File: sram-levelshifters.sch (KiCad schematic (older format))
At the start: 15 parts, among them U10 TXB0108-PW, U11 ISSI61WV5128BL, U12 ISSI61WV5128BL, U13 ISSI61WV5128BL, U14 ISSI61WV5128BL, U4 TXB0108-PW, U5 TXB0108-PW, U6 TXB0108-PW, U7 74HC04, U8 TXB0108-PW, U9 74LS32

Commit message: Revised logic using nOE and R/nW as supposed to be...
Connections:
- net mR/~W: now also U7.3
- net ~mOE: now reaches U7.4
- net ~mOE: now also U11.24 (~OE), U12.24 (~OE), U13.24 (~OE), U14.24 (~OE)
- removed net ~ADDRESS_SELECTOR: U11.24 (~OE), U12.24 (~OE), U13.24 (~OE), U14.24 (~OE), U9.3
- new net ~ADDRSEL16K: U9.3
- no-connect marks 31 -> 29
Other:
- moved on the sheet: U7B, U7C, U7D, U7E, U7F
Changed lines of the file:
@@
 Text Notes 6450 800  0    59   ~ 12
 STATIC RAM
-Text GLabel 8350 2650 3    39   BiDi ~ 8
-~ADDRESS_SELECTOR
-Text GLabel 10000 2650 3    39   BiDi ~ 8
-~ADDRESS_SELECTOR
-Text GLabel 10000 5550 3    39   BiDi ~ 8
-~ADDRESS_SELECTOR
-Text GLabel 8350 5550 3    39   BiDi ~ 8
-~ADDRESS_SELECTOR
 Text GLabel 5000 4100 2    39   BiDi ~ 8
-~ADDRESS_SELECTOR
+~ADDRSEL16K
 $Comp
 L 74LS32 U9
@@
 L 74HC04 U7
 U 2 1 5C2DFEE1
-P 3600 4450
-F 0 "U7" H 3600 4500 50  0000 C CNN
-F 1 "74HC04" H 3600 4400 50  0000 C CNN
-F 2 "Housings_SSOP:TSSOP-14_4.4x5mm_Pitch0.65mm" H 3600 4450 50  0001 C CNN
-F 3 "" H 3600 4450 50  0001 C CNN
-	2    3600 4450
+P 4600 4500
+F 0 "U7" H 4600 4550 50  0000 C CNN
+F 1 "74HC04" H 4600 4450 50  0000 C CNN
+F 2 "Housings_SSOP:TSSOP-14_4.4x5mm_Pitch0.65mm" H 4600 4500 50  0001 C CNN
+F 3 "" H 4600 4500 50  0001 C CNN
+	2    4600 4500
 	1    0    0    -1
 $EndComp
@@
 L 74HC04 U7
 U 3 1 5C2DFF28
-P 4350 4450
-F 0 "U7" H 4350 4500 50  0000 C CNN
-F 1 "74HC04" H 4350 4400 50  0000 C CNN
-F 2 "Housings_SSOP:TSSOP-14_4.4x5mm_Pitch0.65mm" H 4350 4450 50  0001 C CNN
-F 3 "" H 4350 4450 50  0001 C CNN
-	3    4350 4450
-	1    0    0    -1
+P 5850 4800
+F 0 "U7" H 5850 4850 50  0000 C CNN
+F 1 "74HC04" H 5850 4750 50  0000 C CNN
+F 2 "Housings_SSOP:TSSOP-14_4.4x5mm_Pitch0.65mm" H 5850 4800 50  0001 C CNN
+F 3 "" H 5850 4800 50  0001 C CNN
+	3    5850 4800
+	0    1    1    0
 $EndComp
 $Comp
 L 74HC04 U7
 U 4 1 5C2E0001
-P 5100 4450
-F 0 "U7" H 5100 4500 50  0000 C CNN
-F 1 "74HC04" H 5100 4400 50  0000 C CNN
-F 2 "Housings_SSOP:TSSOP-14_4.4x5mm_Pitch0.65mm" H 5100 4450 50  0001 C CNN
-F 3 "" H 5100 4450 50  0001 C CNN
-	4    5100 4450
-	1    0    0    -1
-$EndComp
-NoConn ~ 5400 4450
-NoConn ~ 4800 4450
-NoConn ~ 4650 4450
-NoConn ~ 4050 4450
-NoConn ~ 3900 4450
-NoConn ~ 3300 4450
+P 5850 5550
+F 0 "U7" H 5850 5600 50  0000 C CNN
+F 1 "74HC04" H 5850 5500 50  0000 C CNN
+F 2 "Housings_SSOP:TSSOP-14_4.4x5mm_Pitch0.65mm" H 5850 5550 50  0001 C CNN
+F 3 "" H 5850 5550 50  0001 C CNN
+	4    5850 5550
+	0    1    1    0
+$EndComp
+NoConn ~ 5850 4500
+NoConn ~ 5850 5100
+NoConn ~ 5850 5250
+NoConn ~ 5850 5850
 $Comp
 L 74HC04 U7
 U 5 1 5C2E0114
-P 5800 4550
-F 0 "U7" H 5800 4600 50  0000 C CNN
-F 1 "74HC04" H 5800 4500 50  0000 C CNN
-F 2 "Housings_SSOP:TSSOP-14_4.4x5mm_Pitch0.65mm" H 5800 4550 50  0001 C CNN
-F 3 "" H 5800 4550 50  0001 C CNN
-	5    5800 4550
+P 5850 6300
+F 0 "U7" H 5850 6350 50  0000 C CNN
+F 1 "74HC04" H 5850 6250 50  0000 C CNN
+F 2 "Housings_SSOP:TSSOP-14_4.4x5mm_Pitch0.65mm" H 5850 6300 50  0001 C CNN
+F 3 "" H 5850 6300 50  0001 C CNN
+	5    5850 6300
 	0    1    1    0
 $EndComp
@@
 L 74HC04 U7
 U 6 1 5C2E0161
-P 5750 5400
-F 0 "U7" H 5750 5450 50  0000 C CNN
-F 1 "74HC04" H 5750 5350 50  0000 C CNN
-F 2 "Housings_SSOP:TSSOP-14_4.4x5mm_Pitch0.65mm" H 5750 5400 50  0001 C CNN
-F 3 "" H 5750 5400 50  0001 C CNN
-	6    5750 5400
-	0    1    1    0
-$EndComp
-NoConn ~ 5800 4250
-NoConn ~ 5800 4850
-NoConn ~ 5750 5100
-NoConn ~ 5750 5700
+P 5850 7050
+F 0 "U7" H 5850 7100 50  0000 C CNN
+F 1 "74HC04" H 5850 7000 50  0000 C CNN
+F 2 "Housings_SSOP:TSSOP-14_4.4x5mm_Pitch0.65mm" H 5850 7050 50  0001 C CNN
+F 3 "" H 5850 7050 50  0001 C CNN
+	6    5850 7050
+	0    1    1    0
+$EndComp
+NoConn ~ 5850 6000
+NoConn ~ 5850 6600
+NoConn ~ 5850 6750
+NoConn ~ 5850 7350
 $Comp
 L 74HC04 U7
@@
 Text GLabel 7150 6050 0    39   BiDi ~ 0
 PB4
+Text GLabel 4300 4500 0    39   BiDi ~ 0
+mR/~W
+Text GLabel 4900 4500 2    39   BiDi ~ 0
+~mOE
+Text GLabel 8350 2650 3    39   BiDi ~ 0
+~mOE
+Text GLabel 10000 2650 3    39   BiDi ~ 0
+~mOE
+Text GLabel 10000 5550 3    39   BiDi ~ 0
+~mOE
+Text GLabel 8350 5550 3    39   BiDi ~ 0
+~mOE
 $EndSCHEMATC

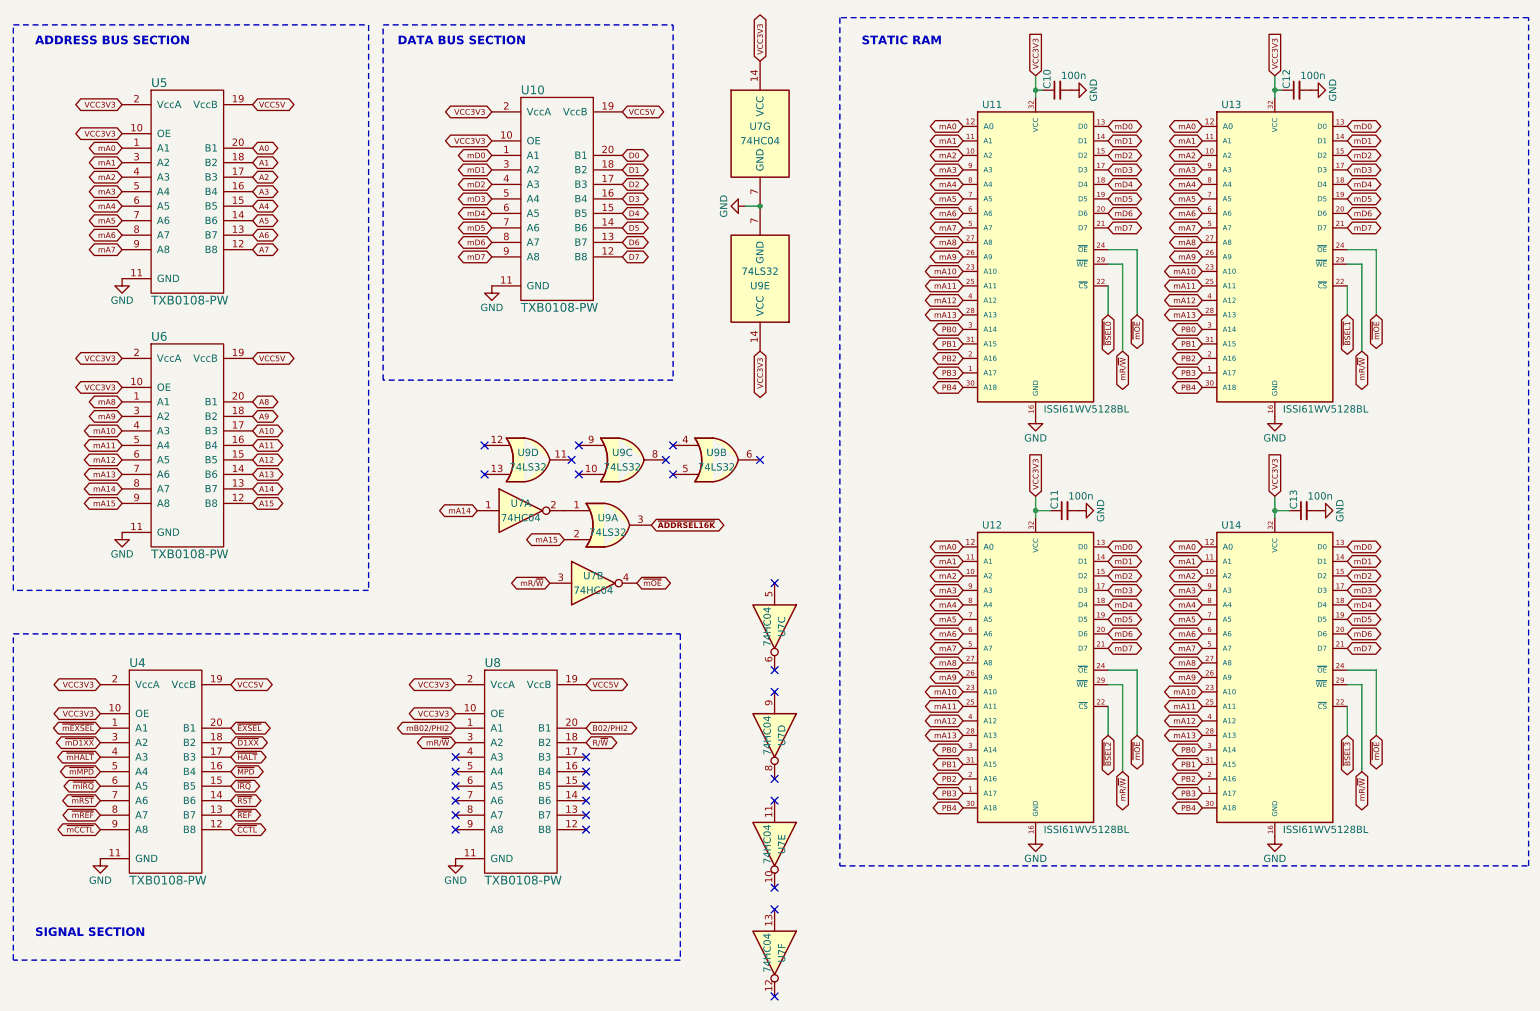
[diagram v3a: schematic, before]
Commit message: Changed the bankselection $D530 and bankcontrol $D531
Changed the bankselection $D530 and bankcontrol $D531
Now in this way, only nCCTL can be used as address selector and only low
byte address is needed in the SoC
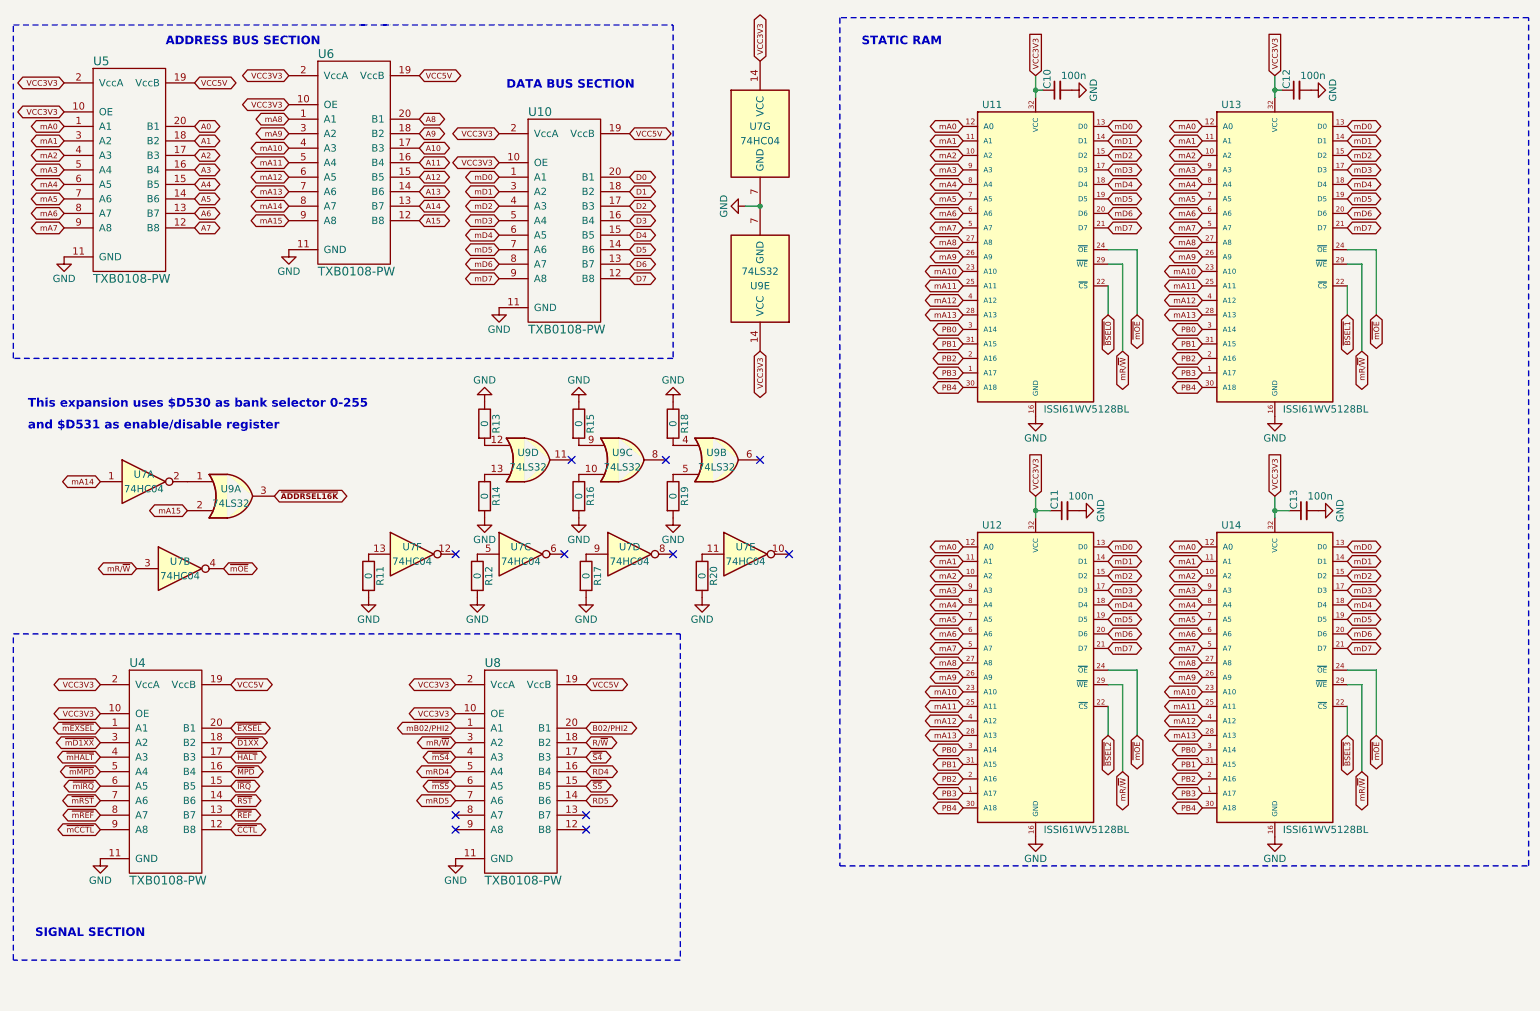
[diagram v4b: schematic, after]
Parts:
- added R11, R12, R13, R14, R15, R16, R17, R18, R19, R20: 0, Resistors_SMD:R_1206_HandSoldering, symbol R
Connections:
- net GND: now also R11.2, R12.2, R13.1, R14.2, R15.1, R16.2, R17.2, R18.1, R19.2, R20.2
- net RD5: now reaches U8.14 (B6)
- net ~S5: now reaches U8.15 (B5)
- net RD4: now reaches U8.16 (B4)
- net ~S4: now reaches U8.17 (B3)
- net ~mS4: now reaches U8.4 (A3)
- net mRD4: now reaches U8.5 (A4)
- net ~mS5: now reaches U8.6 (A5)
- net mRD5: now reaches U8.7 (A6)
- net at U9.4: now also R18.2
- net at U9.5: now also R19.1
- net at U9.10: now also R16.1
- net at U9.9: now also R15.2
- net at U9.12: now also R13.2
- net at U9.13: now also R14.1
- net at U7.5: now also R12.1
- net at U7.9: now also R17.1
- net at U7.11: now also R20.1
- net at U7.13: now also R11.1
- no-connect marks 29 -> 11
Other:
- note added: "This expansion uses $D530 as bank selector 0-255"
- note added: "and $D531 as enable/disable register"
- moved on the sheet: U10, U5, U7A, U7B, U7C, U7D, U7E, U7F, U9A
